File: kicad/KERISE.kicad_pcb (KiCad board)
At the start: 2 copper layers, 40 x 44 mm, 106 parts, among them J1 Motor_L, J10 ENC_Slave, J11 ENC_Host, J12 ENC_Slave, J13 Host, J14 Slave, J15 Host, J16 Slave, J2 Motor_R, J3 Host, J4 Slave, J5 Host, J6 Slave, J7 COM, J8 Fan, J9 ENC_Host, P1 ToF_Host, P2 ToF_Slave, Q1 MTM231232LBF, Q10 SFH3015FA, Q11 MTM231232LBF, Q12 DMN3065LW-7, Q13 SFH3015FA, Q14 DMN3065LW-7, Q2 DMN3065LW-7, Q3 SFH3015FA, Q4 MTM231232LBF, Q5 DMN3065LW-7, Q6 SFH3015FA, Q7 DMN3065LW-7, Q8 MTM231232LBF, Q9 DMN3065LW-7, SW1 RESET, SW2 UPLOAD, U1 ESP32-PICO-D4, U2 DRV8835, U3 LXDC2UR30, U4 AS5048A, U5 AS5048A, U6 ICM-20602, U7 ICM-20602, U8 PCA9632, U9 VL6180X

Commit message: 配置を改良
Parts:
- moved L3 7.63 mm to (158.0, 109.0), turned to 180 degrees
- moved C24 5.02 mm to (136.0, 99.5)
- moved C1 1.90 mm to (143.2, 117.8), turned to 0 degrees
- moved C11 1.68 mm to (134.7, 114.0), turned to 0 degrees
- moved C18 1.68 mm to (163.7, 114.0), turned to 0 degrees
- moved C20 1.68 mm to (163.7, 104.5), turned to 0 degrees
- moved C9 1.68 mm to (134.7, 104.5), turned to 0 degrees
- moved U3 0.75 mm to (143.2, 116.2)
- moved U8 0.71 mm to (139.0, 98.5), turned to 225 degrees
- moved C10 0.50 mm to (135.0, 108.0), turned to 270 degrees
- moved C12 0.50 mm to (135.0, 117.5), turned to 270 degrees
- moved C19 0.50 mm to (164.0, 117.5), turned to 270 degrees
- moved C21 0.50 mm to (164.0, 108.0), turned to 270 degrees
- moved R11 0.25 mm to (162.0, 115.5)
- moved R13 0.25 mm to (162.0, 106.0)
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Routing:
- net +BATT: track 42.5 -> 40.2 mm
- net +3V3: track 2.69 -> 3.97 mm
- net GND: track 35.1 -> 35.7 mm

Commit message: フットプリントを改良
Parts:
- Q1, Q11, Q12, Q2, Q4, Q5, Q8, Q9: footprint TO_SOT_Packages_SMD:SOT-323_SC-70 -> mouse:SOT-323_SC-70
- Q14, Q7: footprint TO_SOT_Packages_SMD:SOT-323_SC-70 -> Package_TO_SOT_SMD:SOT-323_SC-70
- moved R19 2.00 mm to (161.0, 99.5), turned to 270 degrees
- moved C2 0.50 mm to (142.0, 94.0)
- moved C7 0.50 mm to (155.0, 94.0)

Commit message: 自動配線成功
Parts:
- moved R4 1.41 mm to (139.5, 91.5), turned to 0 degrees
- moved R5 1.41 mm to (157.5, 91.5), turned to 0 degrees
- moved D2 0.72 mm to (157.0, 90.5), turned to 180 degrees
- moved D1 0.71 mm to (140.0, 90.5), turned to 180 degrees
- moved C3 0.50 mm to (155.5, 118.8)
- moved C4 0.50 mm to (154.0, 118.8)
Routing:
- net /IR_RCV_SR/LED_to_C: track 0.00 -> 2.41 mm, vias 0 -> 1
- net /IR_RCV_SL/LED_to_C: track 0.00 -> 2.41 mm, vias 0 -> 1

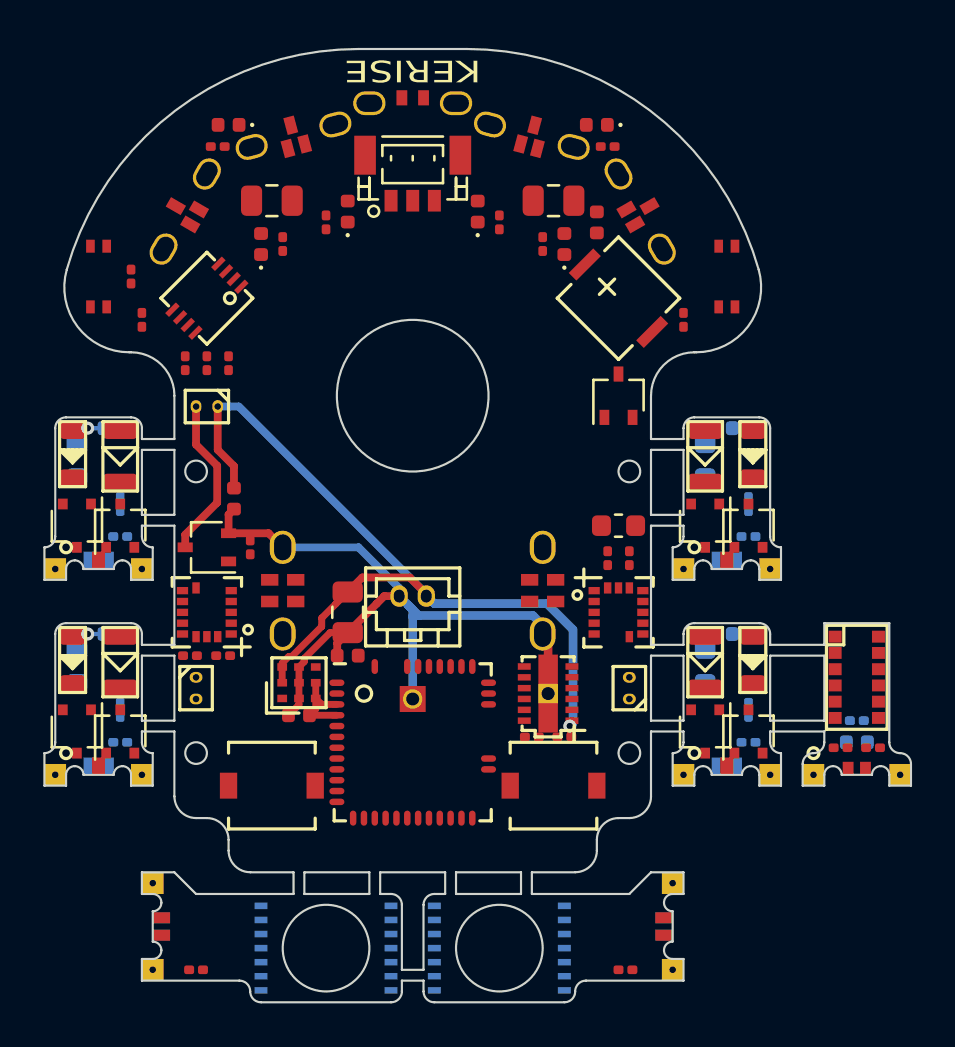
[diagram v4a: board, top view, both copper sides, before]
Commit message: アンテナを外側に配置
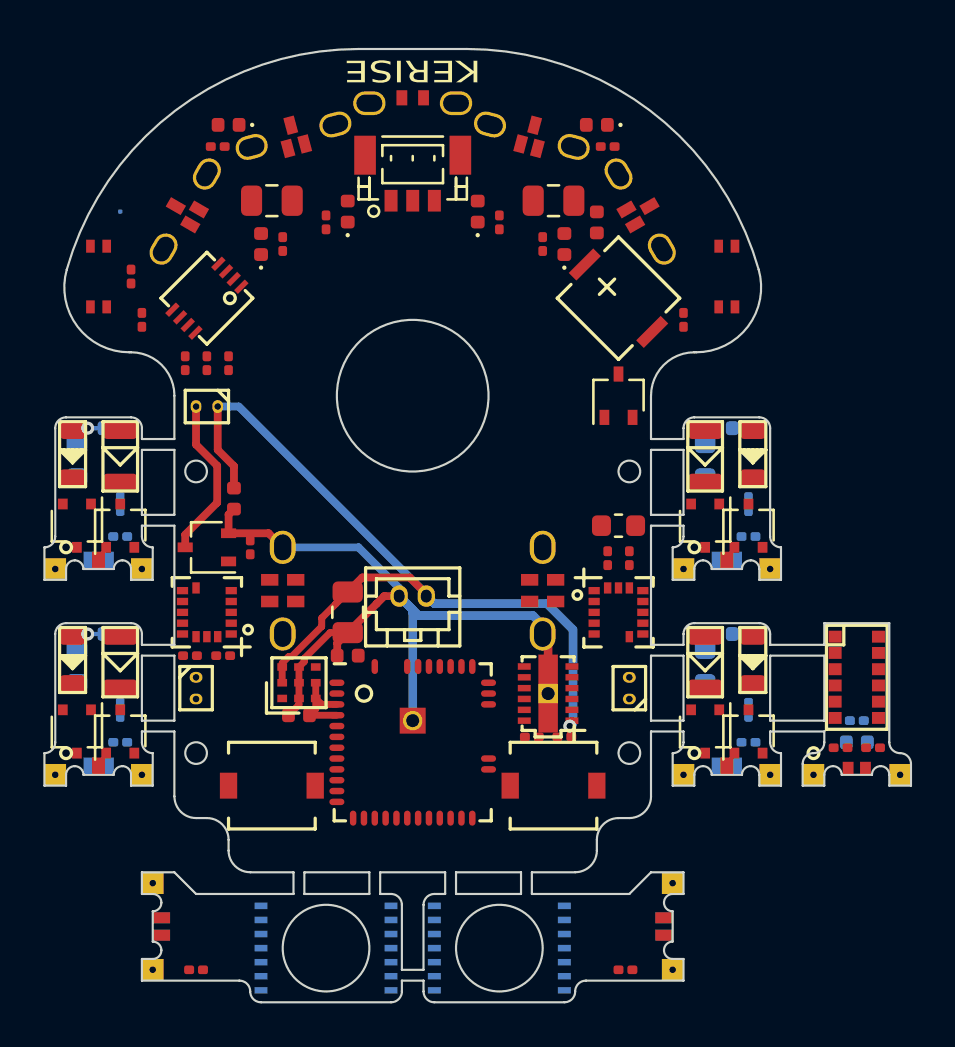
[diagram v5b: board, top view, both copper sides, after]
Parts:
- added AE1: Antenna, mouse:HIDDEN_PAD, B.Cu at (135.0, 94.5)
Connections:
- U1 pad 2: (no net) -> /ANTENA
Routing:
- net GND: track 35.7 -> 38.9 mm
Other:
- net class Antena: clearance 0.15 -> 0.18; trace_width 0.2 -> 0.15

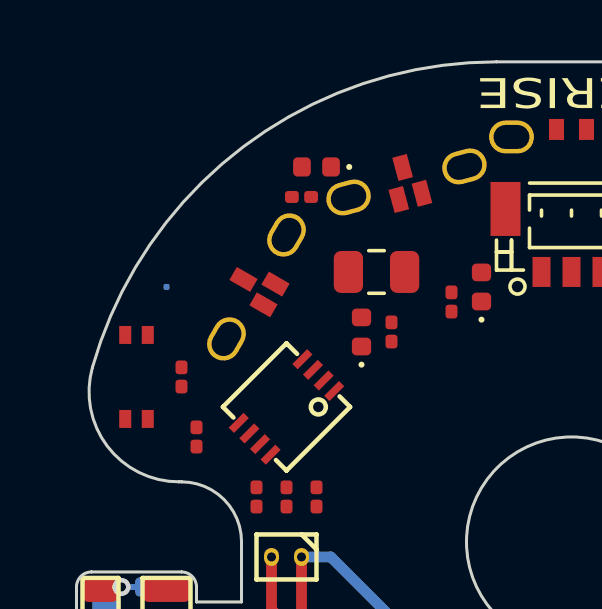
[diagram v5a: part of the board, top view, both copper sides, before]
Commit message: デザインルールを緩和
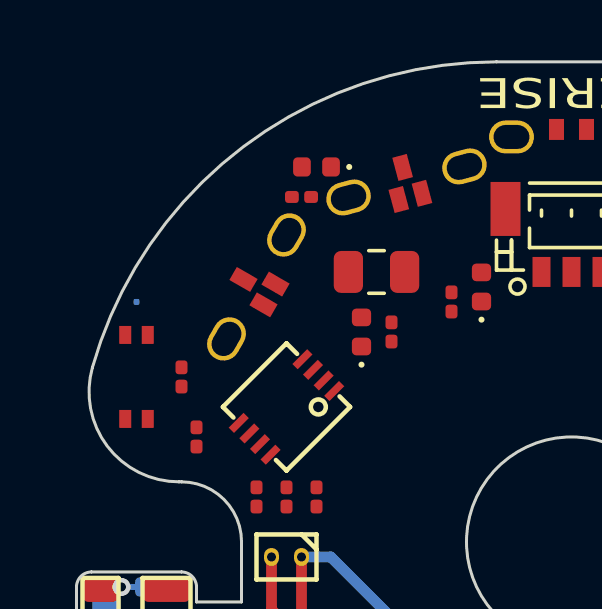
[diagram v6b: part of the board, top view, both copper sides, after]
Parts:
- moved AE1 1.12 mm to (134.0, 95.0)
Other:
- net class Antena: clearance 0.18 -> 0.15
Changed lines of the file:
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@@
   )
   (setup
-    (last_trace_width 0.4)
+    (last_trace_width 0.15)
     (user_trace_width 0.15)
     (user_trace_width 0.2)
@@
   )
   (net_class Antena ""
-    (clearance 0.18)
+    (clearance 0.15)
     (trace_width 0.15)
     (via_dia 0.6)
@@
   )
   (module mouse:HIDDEN_PAD (layer B.Cu)
-    (at 135 94.5)
+    (at 134 95)
     (fp_text reference AE1 (at 0 -0.5) (layer B.SilkS) hide
       (effects (font (size 1 1) (thickness 0.15)) (justify mirror))

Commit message: 3Dシェイプを割り当て
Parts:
- moved AE1 29.0 mm to (163.0, 95.0)

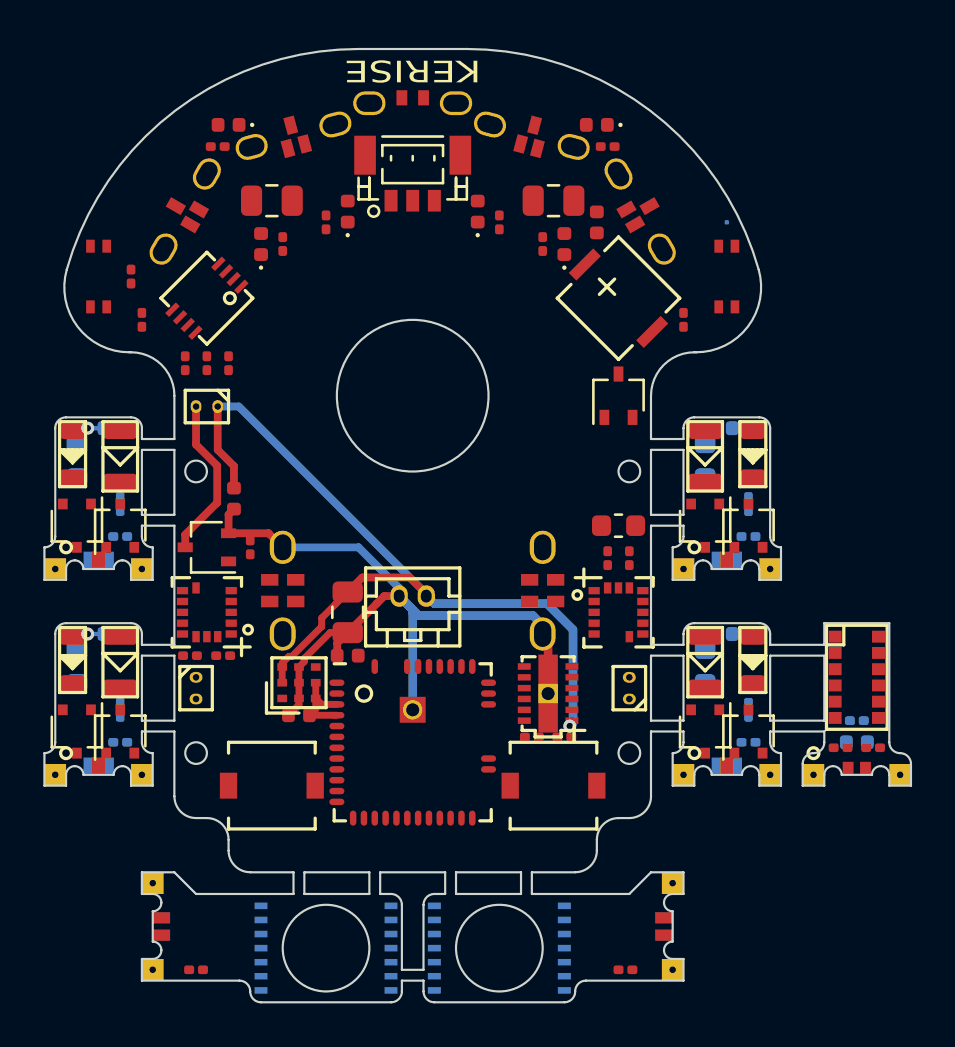
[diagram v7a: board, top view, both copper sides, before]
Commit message: 以前成功した自動配線を適用，基板発注
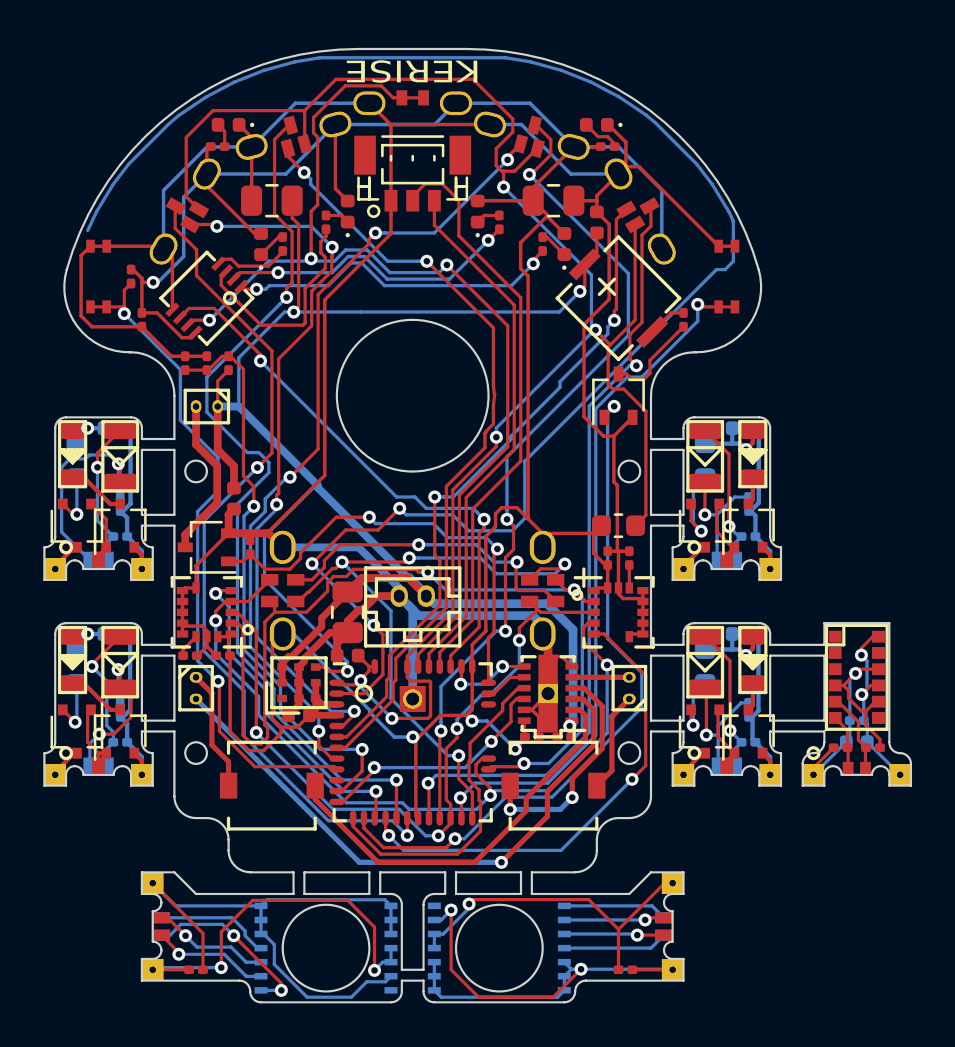
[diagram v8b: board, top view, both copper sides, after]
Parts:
- removed AE1: Antenna, mouse:HIDDEN_PAD
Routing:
- net +3V3: track 3.97 -> 129.0 mm, vias 0 -> 4
- net GND: track 38.5 -> 156.4 mm
- net VDDA: track 0.00 -> 82.3 mm, vias 0 -> 5
- net /ANTENA: track 0.00 -> 74.4 mm, vias 0 -> 3
- net I2C-SDA: track 0.00 -> 48.2 mm, vias 0 -> 3
- net SPI-SCLK: track 0.00 -> 42.8 mm, vias 0 -> 3
- net +BATT: track 40.0 -> 82.3 mm, vias 1 -> 4
- net PR-LED-FL: track 0.00 -> 40.9 mm, vias 0 -> 2
- net PR-LED-FR: track 0.00 -> 38.8 mm, vias 0 -> 4
- net PR-LED-SL: track 0.00 -> 38.6 mm, vias 0 -> 2
- net PR-RCV-FR: track 0.00 -> 37.0 mm, vias 0 -> 4
- net SPI-MISO: track 0.00 -> 36.3 mm, vias 0 -> 3
- net PR-LED-SR: track 0.00 -> 36.0 mm, vias 0 -> 2
- net PR-RCV-FL: track 0.00 -> 35.9 mm, vias 0 -> 2
- net PR-RCV-SL: track 0.00 -> 33.5 mm, vias 0 -> 4
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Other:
- board text added: "2019.01.06"
- board text removed: "2019.01.01"
